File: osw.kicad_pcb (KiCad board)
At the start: 4 copper layers, 45 x 41 mm, 56 parts, among them J1 Conn_01x02, J2 Conn_01x04, J3 Conn_01x02, Q1 2N7002, SW1 SW_Push, SW2 SW_Push, SW4 SW_Push, SW5 SW_Push, U1 DS3231MZ, U10 LTC3440EMS, U11 MCP73831T-2ACI_OT, U2 BMA400, U3 BMP280, U4 GC9A01_IPS_display, U5 USB-OTG, U6 CH340E, U7 ttgo-32-micro, U8 Quectel_L96, U9 TPS2115A

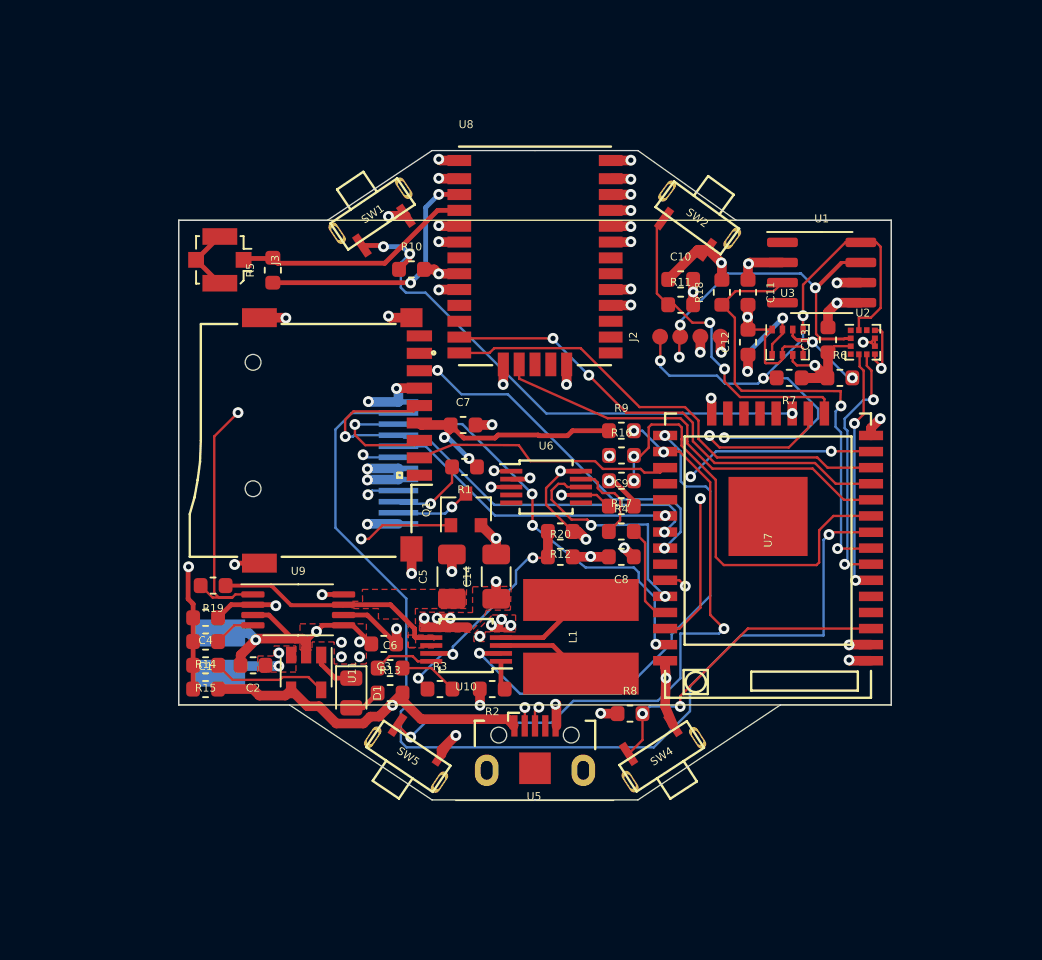
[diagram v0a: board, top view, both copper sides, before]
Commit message: update PCB, place components randomly
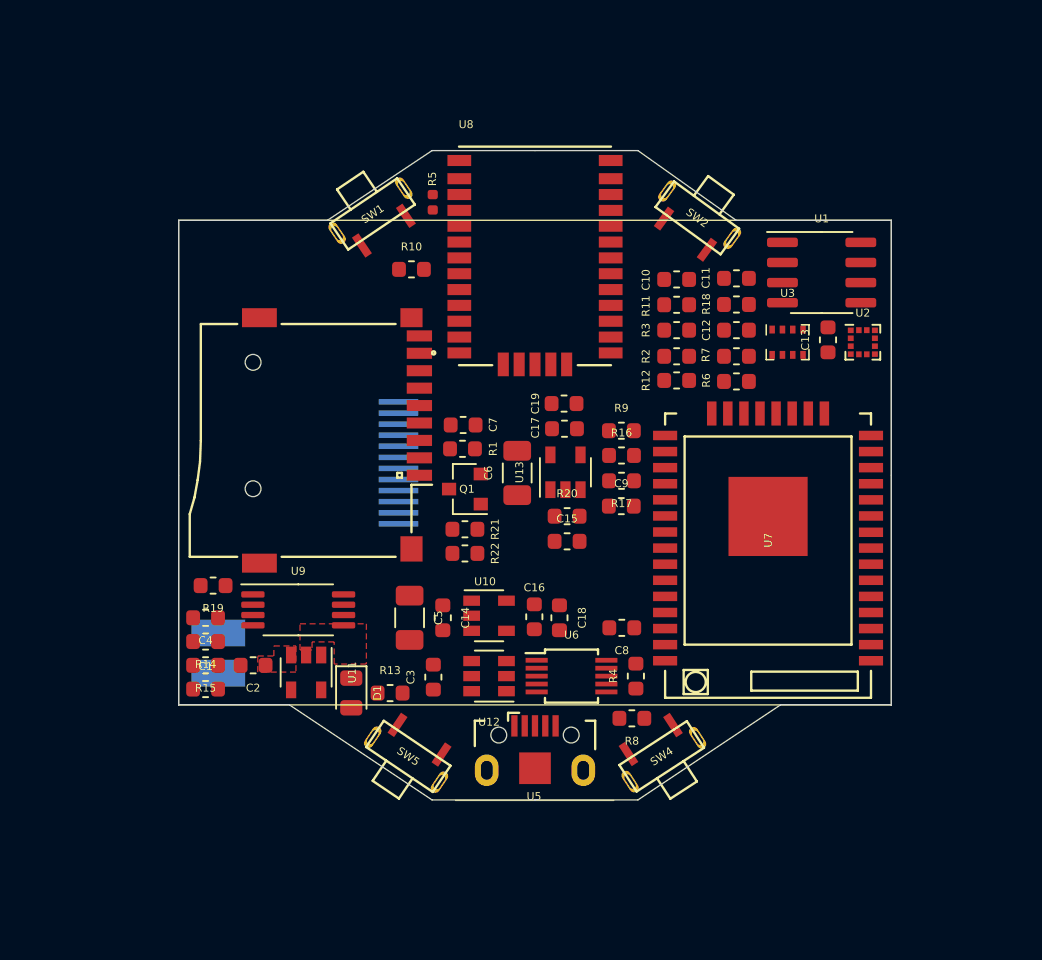
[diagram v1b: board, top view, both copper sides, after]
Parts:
- removed J2: Conn_01x04, Connector_PinHeader_1.27mm:PinHeader_1x04_P1.27mm_Vertical
- removed J3: Conn_01x02, open-Smartwatch:U.FL_Molex_MCRF_73412-0110_Vertical
- removed L1: 10uH, open-Smartwatch:L_Sumida-CDRH6D38
- added C15: 0.1u, Capacitor_SMD:C_0603_1608Metric, F.Cu at (162.0, 114.2)
- added C16: 4.7u, Capacitor_SMD:C_0603_1608Metric, F.Cu at (160.0, 118.9)
- added C17: 4.7u, Capacitor_SMD:C_0603_1608Metric, F.Cu at (161.9, 107.1)
- added C18: 0.1u, Capacitor_SMD:C_0603_1608Metric, F.Cu at (161.5, 119.0)
- added C19: 0.1u, Capacitor_SMD:C_0603_1608Metric, F.Cu at (161.8, 105.5)
- added R21: 10k, Resistor_SMD:R_0603_1608Metric, F.Cu at (155.6, 113.4)
- added R22: 1M, Resistor_SMD:R_0603_1608Metric, F.Cu at (155.6, 114.9)
- added U12: USBLC6-2SC6, Package_TO_SOT_SMD:SOT-23-6, F.Cu at (157.1, 122.7)
- added U13: XC6209, Package_TO_SOT_SMD:SOT-23-5, F.Cu at (161.9, 109.8)
- C14: value 22uF -> 0.1u; footprint Capacitor_SMD:C_1206_3216Metric -> Capacitor_SMD:C_0603_1608Metric
- C5: value 10uF -> 100u
- C6: value 150pF -> 100u; footprint Capacitor_SMD:C_0603_1608Metric -> Capacitor_SMD:C_1206_3216Metric
- R12: value 340k -> 5.6k
- R16: value 10M -> 1M
- R17: value 2.2M -> 220k
- R2: value 60.4k -> 1k
- R20: value 200k -> 2.2K
- R3: value 15k -> 1k
- R5: footprint Resistor_SMD:R_0603_1608Metric -> Resistor_SMD:R_0402_1005Metric
- R6, R7: value 2.2k -> 1k
- U10: value LTC3440EMS -> XC6209; footprint Package_SO:MSOP-10_3x3mm_P0.5mm -> Package_TO_SOT_SMD:SOT-23-5
- moved R3 27.1 mm to (168.9, 100.8)
- moved R2 24.0 mm to (168.9, 102.5), turned to 0 degrees
- moved C6 14.7 mm to (158.9, 109.9), turned to 90 degrees
- moved U6 12.0 mm to (162.3, 122.7)
- moved R12 12.0 mm to (168.9, 104.0)
- moved R5 11.0 mm to (153.5, 92.8), turned to 270 degrees
- moved R4 9.18 mm to (166.4, 122.7), turned to 90 degrees
- moved R6 6.53 mm to (172.7, 104.1)
- moved C8 4.48 mm to (165.5, 119.6)
- moved C14 4.26 mm to (154.2, 119.0), turned to 270 degrees
- moved C3 3.77 mm to (153.6, 122.7), turned to 90 degrees
- moved C5 3.72 mm to (152.1, 119.0), turned to 270 degrees
- moved R7 3.60 mm to (172.7, 102.5)
- moved R20 2.60 mm to (162.0, 112.6)
- moved U10 2.37 mm to (157.1, 118.9), turned to 0 degrees
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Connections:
- C10 pad 1: +3V3 -> /3V3_2
- C14 pad 1: +3V3 -> /VCC
- C5 pad 1: /VOUT -> /VCC
- C6 pad 1: Net-(C6-Pad1) -> /VCC
- C6 pad 2: Net-(C6-Pad2) -> GND
- Q1 pad 1: /PIN_LED -> Net-(Q1-Pad1)
- R1 pad 1: +3V3 -> /3V3_2
- R12 pad 1: +3V3 -> GND
- R12 pad 2: Net-(R12-Pad2) -> /GPS_RX2V8
- R19 pad 1: /VOUT -> /VCC
- R2 pad 1: Net-(R2-Pad1) -> /GPS_RX2V8
- R2 pad 2: GND -> /GPS_RX3V3
- R20 pad 1: Net-(R12-Pad2) -> /VCC
- R20 pad 2: GND -> /PWR2_EN
- R3 pad 1: Net-(R12-Pad2) -> /GPS_TX2V8
- R3 pad 2: Net-(C6-Pad2) -> /GPS_TX3V3
- U10 pad 1: Net-(R2-Pad1) -> /VCC
- U10 pad 2: /MODE_SYNC -> GND
- U10 pad 3: Net-(L1-Pad1) -> /VCC
- U10 pad 5: GND -> +3V3
- U4 pad 4: +3V3 -> /3V3_2
- U5 pad 3: /D_P -> /D2_P
- U5 pad 4: /D_N -> /D2_N
- U6 pad 1: /D_P -> /D1_P
- U6 pad 2: /D_N -> /D1_N
- U7 pad 11: /GPS_FON -> Net-(U7-Pad11)
- U7 pad 12: /GPS_TX -> /GPS_TX3V3
- U7 pad 13: /GPS_RX -> /GPS_RX3V3
- U7 pad 24: /MODE_SYNC -> /PWR2_EN
- U8 pad 25: /GPS_TX -> /GPS_TX2V8
- U8 pad 26: /GPS_RX -> /GPS_RX2V8
- U8 pad 28: /GPS_FON -> Net-(U8-Pad28)
- U8 pad 8: +3V3 -> /3V3_2
- U8 pad 9: +3V3 -> /3V3_2
- U9 pad 7: /VOUT -> /VCC
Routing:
- net GND: track 103.9 -> 0.00 mm, vias 51 -> 0
- net +3V3: track 73.1 -> 0.00 mm, vias 24 -> 0
- net /TFT_RST: track 66.0 -> 0.00 mm, vias 1 -> 0
- net /SDA: track 63.5 -> 0.00 mm, vias 6 -> 0
- net /SCL: track 55.5 -> 0.00 mm, vias 5 -> 0
- net /STAT_PWR: track 48.5 -> 0.00 mm, vias 2 -> 0
- net /PIN_LED: track 43.8 -> 0.00 mm, vias 2 -> 0
- net /FLASH: track 41.3 -> 0.00 mm, vias 4 -> 0
- net /VBAT: track 39.2 -> 0.00 mm, vias 5 -> 0
- net /TFT_DC: track 37.1 -> 0.00 mm, vias 3 -> 0
- net /BTN2: track 34.9 -> 0.00 mm, vias 3 -> 0
- net /MOSI: track 33.5 -> 0.00 mm, vias 4 -> 0
- net /MODE_SYNC: track 31.9 -> 0.00 mm, vias 2 -> 0
- net /VBUS: track 31.8 -> 0.00 mm, vias 2 -> 0
- net /GPS_TX: track 30.6 -> 0.00 mm, vias 2 -> 0
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- removed copper zone on F.Cu, net +3V3
- removed copper zone on F.Cu, net /VOUT

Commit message: update board to rev2.0
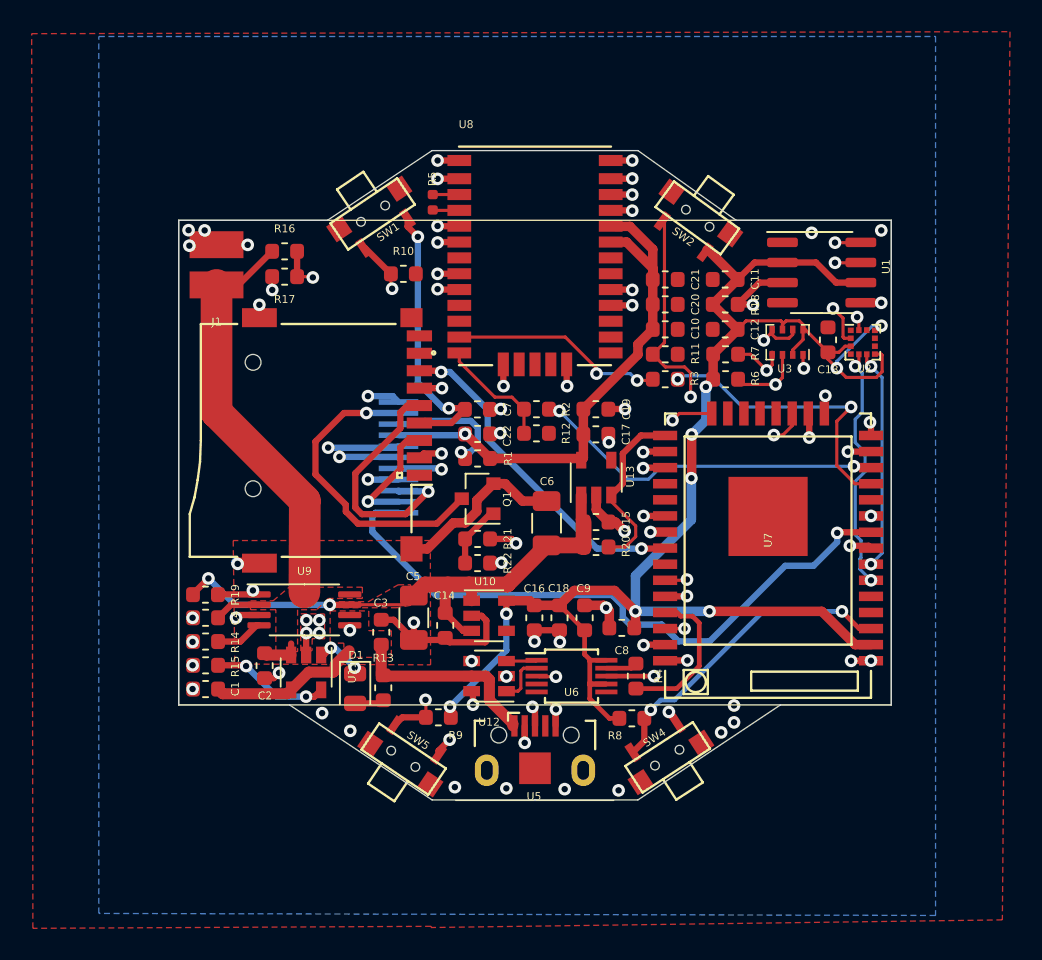
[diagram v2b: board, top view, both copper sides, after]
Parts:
- added C20: 100p, Capacitor_SMD:C_0603_1608Metric, F.Cu at (168.2, 99.2)
- added C21: 10p, Capacitor_SMD:C_0603_1608Metric, F.Cu at (168.2, 97.6)
- added C22: 0.1u, Capacitor_SMD:C_0603_1608Metric, F.Cu at (156.4, 107.4)
- J1: moved to F.Cu
- moved R16 24.9 mm to (144.2, 95.9)
- moved R17 24.9 mm to (144.2, 97.5)
- moved J1 24.5 mm to (139.9, 98.0), turned to 180 degrees
- moved R9 21.5 mm to (153.9, 125.3), turned to 180 degrees
- moved R12 9.46 mm to (160.1, 107.4)
- moved R2 9.46 mm to (160.1, 105.8)
- moved C9 7.42 mm to (163.1, 119.0), turned to 90 degrees
- moved C3 4.34 mm to (150.3, 119.9)
- moved C6 3.68 mm to (160.7, 113.0)
- moved C10 3.23 mm to (168.2, 100.8)
- moved R11 3.21 mm to (168.2, 102.4)
- moved R3 3.18 mm to (168.2, 103.9)
- moved R20 2.67 mm to (163.9, 114.5)
- moved C15 2.20 mm to (163.9, 113.0)
- moved C19 2.04 mm to (163.8, 105.8)
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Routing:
- net +3V3: track 0.00 -> 138.0 mm, vias 0 -> 11
- net GND: track 0.00 -> 89.0 mm, vias 0 -> 69
- net /B_MON: track 0.00 -> 50.3 mm, vias 0 -> 2
- net /SCL: track 0.00 -> 42.2 mm, vias 0 -> 4
- net /TFT_RST: track 0.00 -> 40.7 mm, vias 0 -> 1
- net /STAT_PWR: track 0.00 -> 40.1 mm, vias 0 -> 2
- net /SDA: track 0.00 -> 38.3 mm, vias 0 -> 4
- net /FLASH: track 0.00 -> 37.3 mm, vias 0 -> 2
- net /PIN_LED: track 0.00 -> 36.1 mm, vias 0 -> 2
- net /VCC: track 0.00 -> 35.8 mm, vias 0 -> 2
- net /3V3_2: track 0.00 -> 34.9 mm, vias 0 -> 1
- net /BTN2: track 0.00 -> 33.8 mm, vias 0 -> 2
- net /SCK: track 0.00 -> 33.3 mm, vias 0 -> 2
- net /VBAT: track 0.00 -> 31.5 mm
- net /TFT_DC: track 0.00 -> 30.9 mm, vias 0 -> 2
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- added copper zone on F.Cu, net /VBUS
- added copper zone on F.Cu, net /VCC
- added copper zone on B.Cu, net GND
- removed copper zone on 3V3, net +3V3

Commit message: finalize v2.0
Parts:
- moved R3 8.36 mm to (160.1, 105.9)
- moved R12 1.57 mm to (160.1, 108.9)
- moved R2 1.57 mm to (160.1, 107.4)
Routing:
- net /GPS_TX2V8: track 13.6 -> 6.88 mm, vias 2 -> 0
- net /GPS_TX3V3: track 18.6 -> 23.3 mm
- net /B_MON: track 50.3 -> 47.8 mm
- net /GPS_RX3V3: track 22.5 -> 21.5 mm
- net /GPS_RX2V8: track 7.40 -> 8.34 mm
- net /RTC_INT: track 23.5 -> 24.2 mm, vias 2 -> 3
- net /3V3_2: track 34.9 -> 35.6 mm
- net GND: track 89.0 -> 89.5 mm, vias 69 -> 137

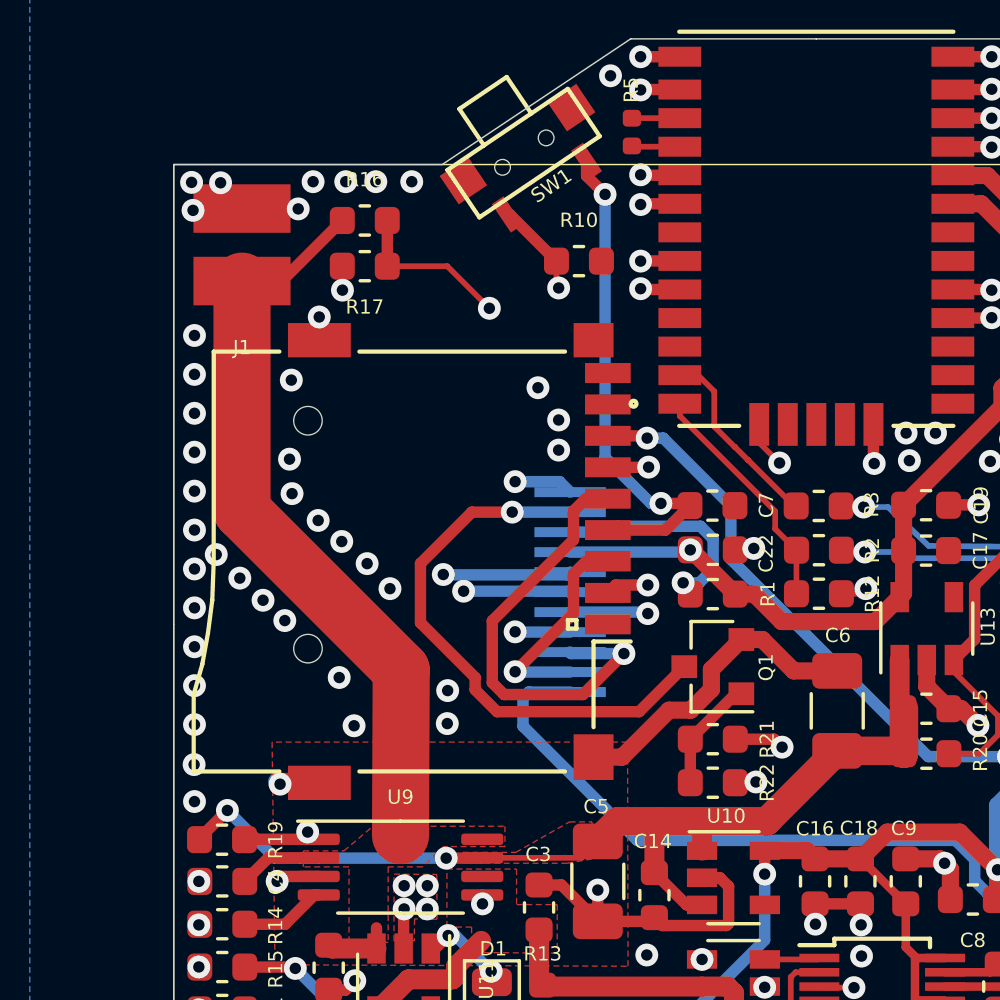
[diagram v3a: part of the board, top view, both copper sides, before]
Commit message: add more silk screen labels
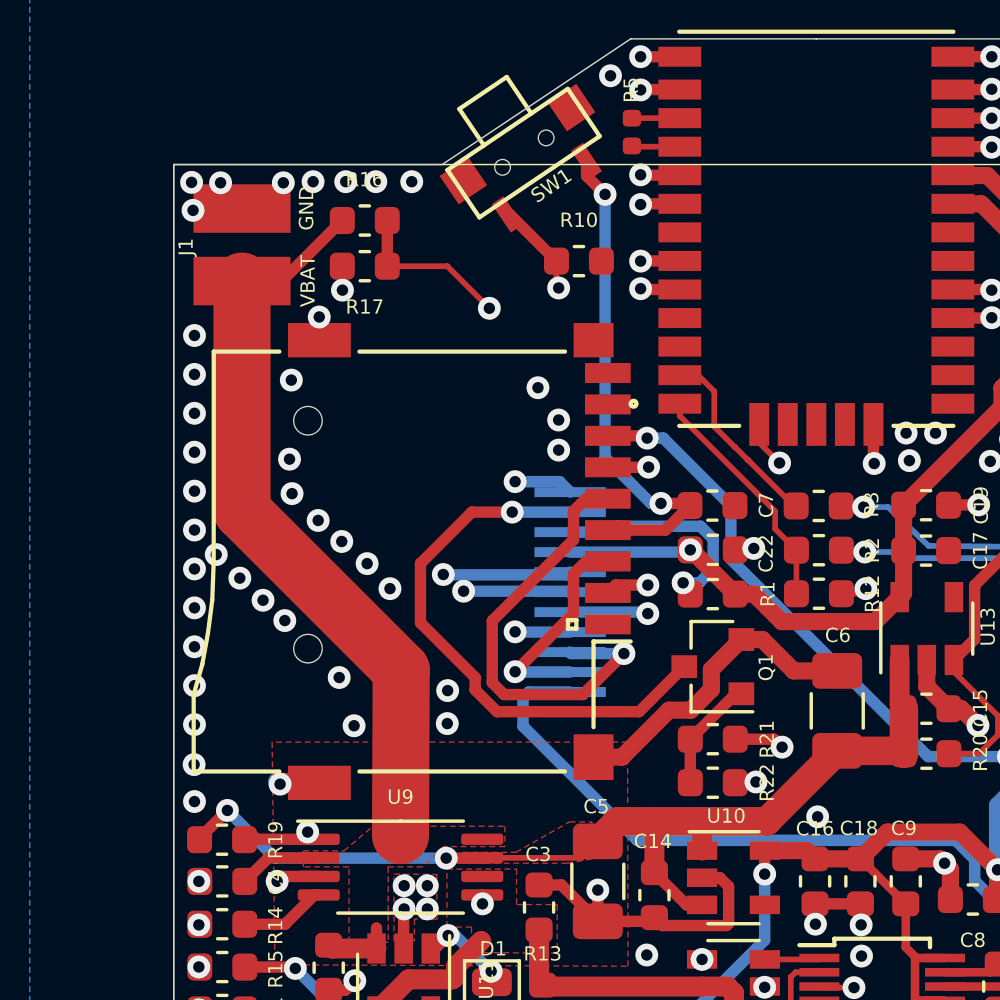
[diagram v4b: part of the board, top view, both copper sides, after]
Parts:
- added G***: LOGO, footprints:p3dt_tiny, B.Cu at (159.9, 94.3)
- added REF**: KiCad-Logo2_5mm_SilkScreen, Symbol:KiCad-Logo2_5mm_SilkScreen, B.Cu at (160.1, 119.8)
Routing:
- net GND: track 89.5 -> 87.5 mm, vias 137 -> 138
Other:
- board text added: "BTN1"
- board text added: "BTN2"
- board text added: "BTN3"
- board text added: "GND"
- board text added: "RESET"
- board text added: "V 2.1"
- board text added: "VBAT"
- board text added: "open-smartwatch.github.io"
- board text added: "pauls_3d_things"
